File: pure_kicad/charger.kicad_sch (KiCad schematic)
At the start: 43 parts, among them J1 XT30M, J2 XT30F, Q1 Q_NMOS_DGS, Q2 Q_NMOS_DGS, Q3 Q_NMOS_DGS, Q4 Q_NMOS_DGS, U1 BQ25756ERRVR

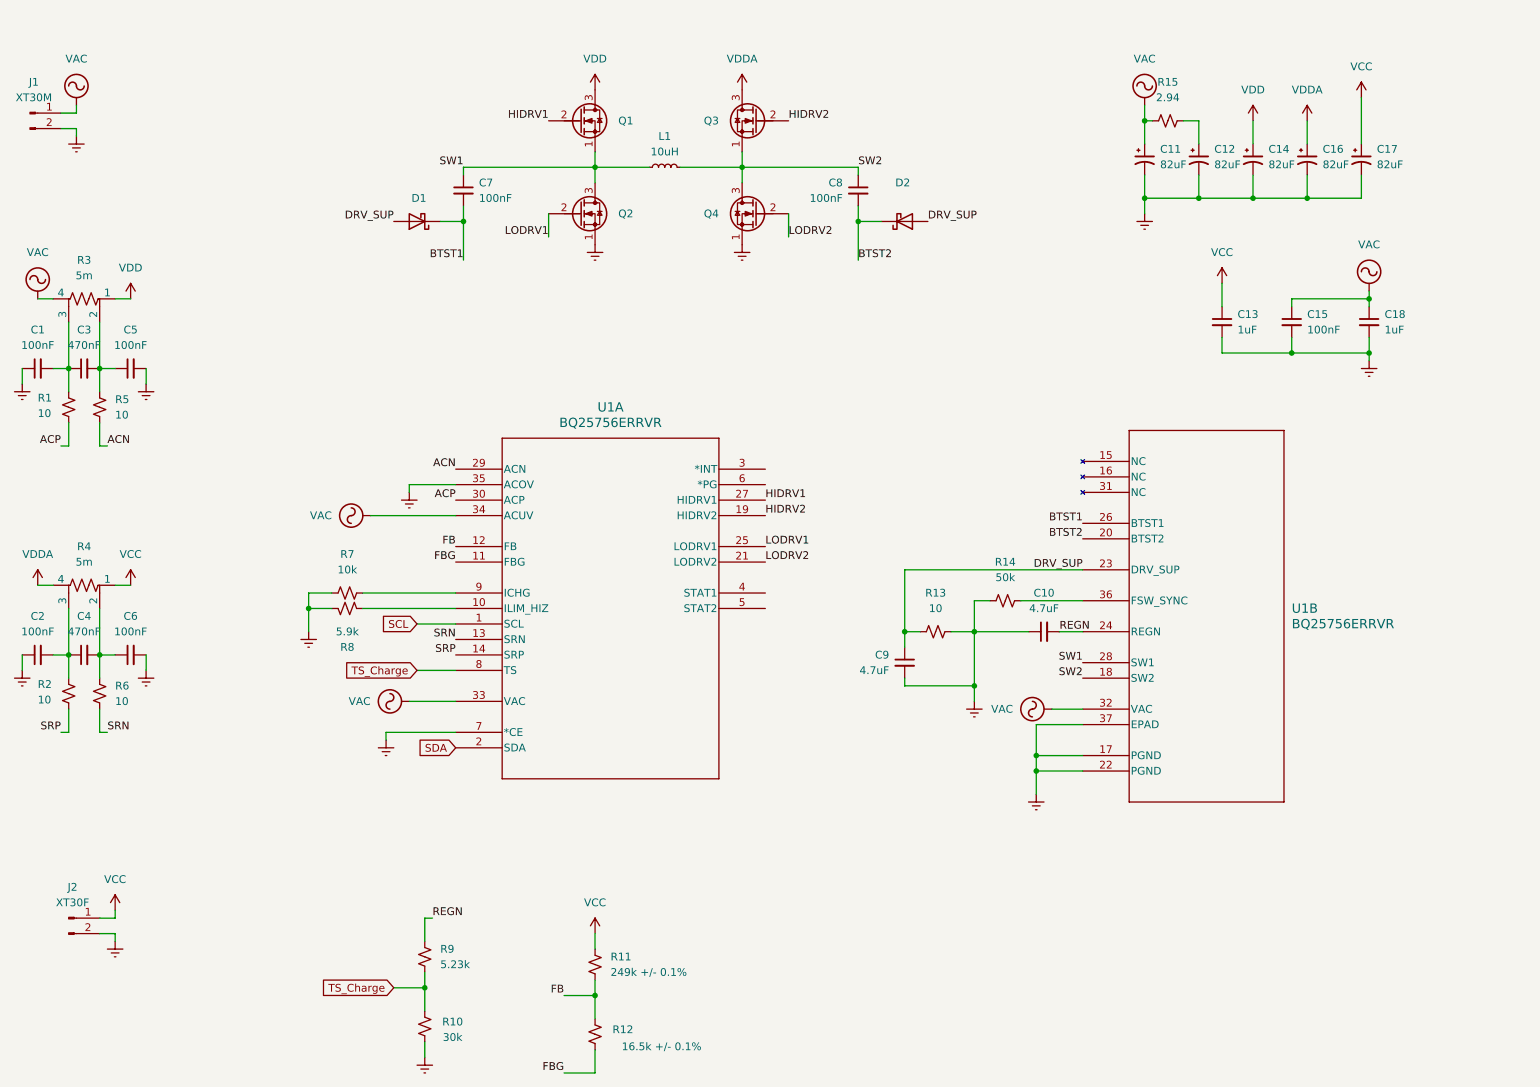
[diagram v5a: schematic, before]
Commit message: So, 10u X5Rs are a thing. Just use 40 of them
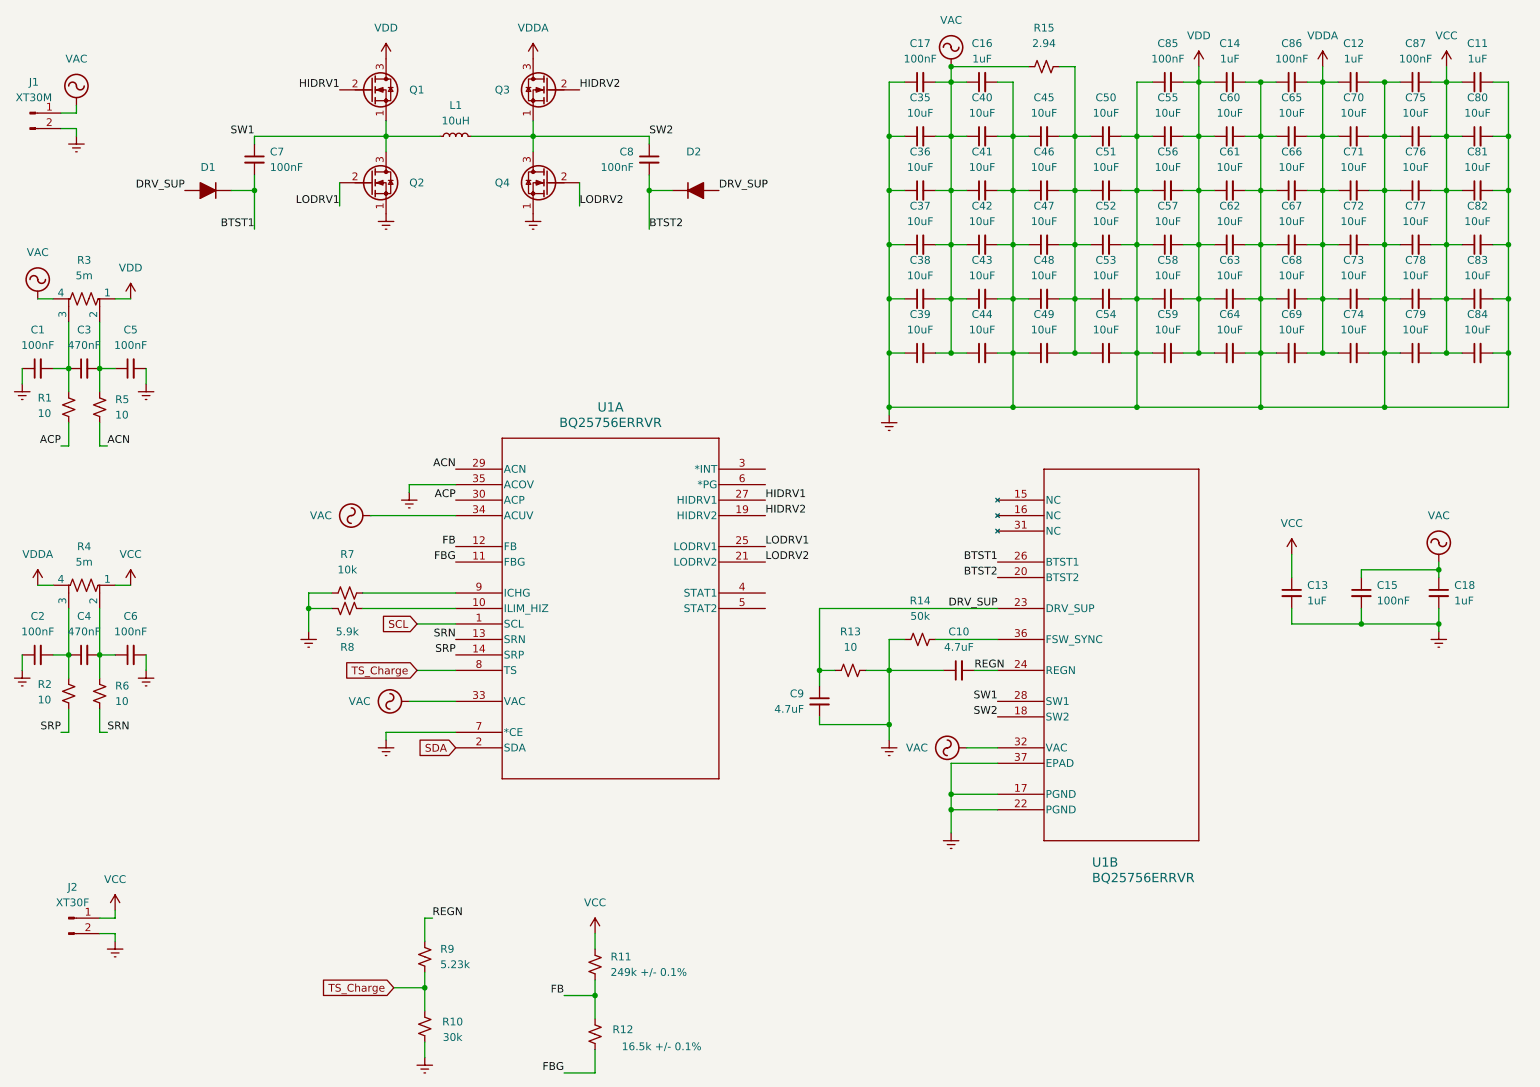
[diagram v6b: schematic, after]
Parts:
- removed C11, C12, C14, C16, C17: 82uF, cyberec:CP_Elec_10x14.3, symbol Device:C_Polarized_Small_US
- added C11, C12, C14, C16: 1uF, cyberec:C_0603_1608Metric_Pad1.08x0.95mm_HandSolder, symbol Device:C_Small
- added C17, C85, C86, C87: 100nF, cyberec:C_0603_1608Metric_Pad1.08x0.95mm_HandSolder, symbol Device:C_Small
- added C35, C36, C37, C38, C39, C40, C41, C42, C43, C44, C45, C46, C47, C48, C49, C50, C51, C52, C53, C54, C55, C56, C57, C58, C59, C60, C61, C62, C63, C64, C65, C66, C67, C68, C69, C70, C71, C72, C73, C74, C75, C76, C77, C78, C79, C80, C81, C82, C83, C84: 10uF, cyberec:C_1206_3216Metric_Pad1.33x1.80mm_HandSolder, symbol Device:C_Small
- D1, D2: symbol Device:D_Schottky -> Device:D_Filled
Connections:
- net Earth: now also C11.2, C12.2, C14.2, C16.2, C17.1, C35.1, C36.1, C37.1, C38.1, C39.1, C40.2, C41.2, C42.2, C43.2, C44.2, C45.1, C46.1, C47.1, C48.1, C49.1, C50.2, C51.2, C52.2, C53.2, C54.2, C55.1, C56.1, C57.1, C58.1, C59.1, C60.2, C61.2, C62.2, C63.2, C64.2, C65.1, C66.1, C67.1, C68.1, C69.1, C70.2, C71.2, C72.2, C73.2, C74.2, C75.1, C76.1, C77.1, C78.1, C79.1, C80.2, C81.2, C82.2, C83.2, C84.2, C85.1, C86.1, C87.1
- net VAC: now also C16.1, C17.2, C35.2, C36.2, C37.2, C38.2, C39.2, C40.1, C41.1, C42.1, C43.1, C44.1
- net VCC: now also C11.1, C75.2, C76.2, C77.2, C78.2, C79.2, C80.1, C81.1, C82.1, C83.1, C84.1, C87.2
- net VDD: now also C14.1, C55.2, C56.2, C57.2, C58.2, C59.2, C60.1, C61.1, C62.1, C63.1, C64.1, C85.2
- net VDDA: now also C12.1, C65.2, C66.2, C67.2, C68.2, C69.2, C70.1, C71.1, C72.1, C73.1, C74.1, C86.2
- net at R15.2: now also C45.2, C46.2, C47.2, C48.2, C49.2, C50.1, C51.1, C52.1, C53.1, C54.1
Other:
- moved on the sheet: C10, C13, C15, C18, C7, C8, C9, L1, Q1, Q2, Q3, Q4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

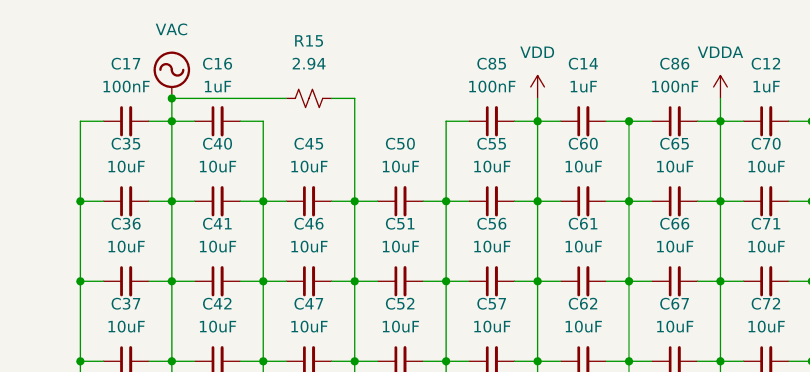
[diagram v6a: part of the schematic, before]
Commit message: Re-layout top side. Bottom to follow
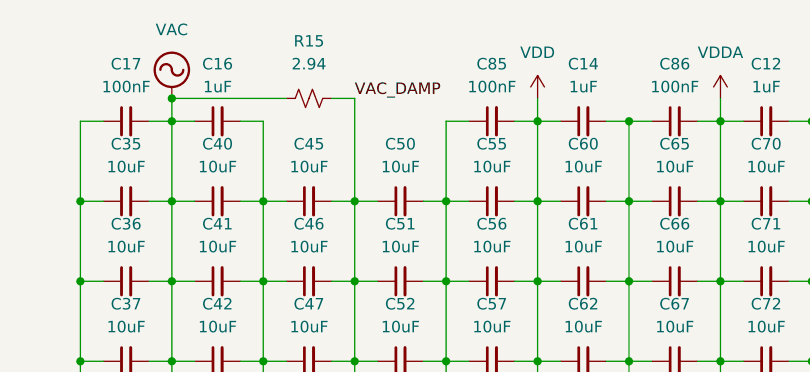
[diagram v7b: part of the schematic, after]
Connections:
- net VAC_DAMP: now reaches C45.2, C46.2, C47.2, C48.2, C49.2, C50.1, C51.1, C52.1, C53.1, C54.1, R15.2
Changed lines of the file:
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@@
+		)
+	)
+	(label "VAC_DAMP"
+		(at 208.28 25.4 0)
+		(effects
+			(font
+				(size 1.27 1.27)
+			)
+			(justify left bottom)
 		)
 	)

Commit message: I think the routing so far is done. I've started collecting signals to route off the board
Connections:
- net nCHRG_INT: now reaches U1.3 (*INT)
- net CHRG_STAT1: now reaches U1.4 (STAT1)
- net CHRG_STAT2: now reaches U1.5 (STAT2)
- net nCHRG_PWR_GOOD: now reaches U1.6 (*PG)
- net VAC_DAMP: no longer names the net of C45.2, C46.2, C47.2, C48.2, C49.2, C50.1, C51.1, C52.1, C53.1, C54.1, R15.2
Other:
- moved on the sheet: C10, C13, C15, C18, C9, R13, R14, U1B
